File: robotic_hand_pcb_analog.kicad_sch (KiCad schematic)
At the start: 0 parts

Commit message: Add WIP schematic changes
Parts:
- added C25, C26, C28, C29, C30, C31, C32: 100n, Capacitor_SMD:C_0603_1608Metric, symbol Device:C
- added C27: 1u, Capacitor_SMD:C_0603_1608Metric, symbol Device:C
- added C33, C34, C35, C36, C37: 1n, Capacitor_SMD:C_0603_1608Metric, symbol Device:C
- added J10: A5, symbol Connector:Conn_01x03_Pin
- added J11: A6, symbol Connector:Conn_01x03_Pin
- added J12: A7, symbol Connector:Conn_01x03_Pin
- added J13: ISENSE1, Connector_PinHeader_2.54mm:PinHeader_1x02_P2.54mm_Vertical, symbol Connector:Conn_01x02_Pin
- added J14: ISENSE2, Connector_PinHeader_2.54mm:PinHeader_1x02_P2.54mm_Vertical, symbol Connector:Conn_01x02_Pin
- added J15: ISENSE3, Connector_PinHeader_2.54mm:PinHeader_1x02_P2.54mm_Vertical, symbol Connector:Conn_01x02_Pin
- added J16: ISENSE4, Connector_PinHeader_2.54mm:PinHeader_1x02_P2.54mm_Vertical, symbol Connector:Conn_01x02_Pin
- added J17: ISENSE5, Connector_PinHeader_2.54mm:PinHeader_1x02_P2.54mm_Vertical, symbol Connector:Conn_01x02_Pin
- added J6: A1, symbol Connector:Conn_01x03_Pin
- added J7: A2, symbol Connector:Conn_01x03_Pin
- added J8: A3, symbol Connector:Conn_01x03_Pin
- added J9: A4, symbol Connector:Conn_01x03_Pin
- added TP1, TP2, TP3, TP4, TP5: TestPoint, TestPoint:TestPoint_Pad_D2.0mm, symbol Connector:TestPoint
- added U10, U11, U12, U13, U9: ACS712xLCTR-05B, Package_SO:SOIC-8_3.9x4.9mm_P1.27mm, symbol Sensor_Current:ACS712xLCTR-05B
- added U8: ADS114S08, adc:ads114s08_tqfp-32, symbol adc:ads114s08
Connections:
- new net: C34.1, U10.6 (FILTER)
- new net: C36.1, U12.6 (FILTER)
- new net: C37.1, U13.6 (FILTER)
- new net: C35.1, U11.6 (FILTER)
- new net: C33.1, U9.6 (FILTER)
- new net: C27.1, U8.23 (REFOUT)
- new net +3V3: C26.2, U8.15 (IOVDD), U8.16 (DVDD)
- new net +5V: C25.2, C28.2, C29.2, C30.2, C31.2, C32.2, J10.2 (Pin_2), J11.2 (Pin_2), J12.2 (Pin_2), J13.1 (Pin_1), J13.2 (Pin_2), J14.1 (Pin_1), J14.2 (Pin_2), J15.1 (Pin_1), J15.2 (Pin_2), J16.1 (Pin_1), J16.2 (Pin_2), J17.1 (Pin_1), J17.2 (Pin_2), J6.2 (Pin_2), J7.2 (Pin_2), J8.2 (Pin_2), J9.2 (Pin_2), U10.1 (IP+), U10.2 (IP+), U10.3 (IP-), U10.4 (IP-), U10.8 (VCC), U11.1 (IP+), U11.2 (IP+), U11.3 (IP-), U11.4 (IP-), U11.8 (VCC), U12.1 (IP+), U12.2 (IP+), U12.3 (IP-), U12.4 (IP-), U12.8 (VCC), U13.1 (IP+), U13.2 (IP+), U13.3 (IP-), U13.4 (IP-), U13.8 (VCC), U8.26 (AVDD), U9.1 (IP+), U9.2 (IP+), U9.3 (IP-), U9.4 (IP-), U9.8 (VCC)
- new net ADC1: TP1.1, U8.7 (AIN0), U9.7 (VIOUT)
- new net ADC10: J10.1 (Pin_1), U8.21 (GPIO1/AIN9)
- new net ADC11: J11.1 (Pin_1), U8.20 (GPIO2/AIN10)
- new net ADC12: J12.1 (Pin_1), U8.19 (GPIO3/AIN11)
- new net ADC2: TP2.1, U10.7 (VIOUT), U8.6 (AIN1)
- new net ADC3: TP3.1, U11.7 (VIOUT), U8.5 (AIN2)
- new net ADC4: TP4.1, U12.7 (VIOUT), U8.4 (AIN3)
- new net ADC5: TP5.1, U13.7 (VIOUT), U8.3 (AIN4)
- new net ADC6: J6.1 (Pin_1), U8.2 (AIN5)
- new net ADC7: J7.1 (Pin_1), U8.32 (REFP1_AIN6)
- new net ADC8: J8.1 (Pin_1), U8.31 (REFN1_AIN7)
- new net ADC9: J9.1 (Pin_1), U8.22 (GPIO0/AIN8)
- new net ADC_CS: U8.9 (CS_N)
- new net ADC_DRDY: U8.13 (DRDY_N)
- new net ADC_MISO: U8.12 (DOUT/DRDY_N)
- new net ADC_MOSI: U8.10 (DIN)
- new net ADC_RST: U8.18 (RESET_N)
- new net ADC_SCK: U8.11 (SCLK)
- new net ADC_SYNC: U8.8 (START_SYNC)
- new net GND: C25.1, C26.1, C27.2, C28.1, C29.1, C30.1, C31.1, C32.1, C33.2, C34.2, C35.2, C36.2, C37.2, J10.3 (Pin_3), J11.3 (Pin_3), J12.3 (Pin_3), J6.3 (Pin_3), J7.3 (Pin_3), J8.3 (Pin_3), J9.3 (Pin_3), U10.5 (GND), U11.5 (GND), U12.5 (GND), U13.5 (GND), U8.14 (DGND), U8.17 (CLK), U8.24 (REFCOM), U8.27 (AVSS), U8.28 (AVSS), U9.5 (GND)
- no-connect marks 0 -> 3
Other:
- note added: "Current Sensors"
- note added: "External ADC IC"
- note added: "External Analog Sensor Breakouts"

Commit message: Assign footprints
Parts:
- J10, J11, J12, J6, J7, J8, J9: footprint (none) -> Connector_PinHeader_2.54mm:PinHeader_1x03_P2.54mm_Vertical
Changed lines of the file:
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@@
 			)
 		)
-		(property "Footprint" ""
+		(property "Footprint" "Connector_PinHeader_2.54mm:PinHeader_1x03_P2.54mm_Vertical"
 			(at 257.81 38.1 0)
 			(effects
@@
 			)
 		)
-		(property "Footprint" ""
+		(property "Footprint" "Connector_PinHeader_2.54mm:PinHeader_1x03_P2.54mm_Vertical"
 			(at 105.41 38.1 0)
 			(effects
@@
 			)
 		)
-		(property "Footprint" ""
+		(property "Footprint" "Connector_PinHeader_2.54mm:PinHeader_1x03_P2.54mm_Vertical"
 			(at 156.21 38.1 0)
 			(effects
@@
 			)
 		)
-		(property "Footprint" ""
+		(property "Footprint" "Connector_PinHeader_2.54mm:PinHeader_1x03_P2.54mm_Vertical"
 			(at 207.01 38.1 0)
 			(effects
@@
 			)
 		)
-		(property "Footprint" ""
+		(property "Footprint" "Connector_PinHeader_2.54mm:PinHeader_1x03_P2.54mm_Vertical"
 			(at 181.61 38.1 0)
 			(effects
@@
 			)
 		)
-		(property "Footprint" ""
+		(property "Footprint" "Connector_PinHeader_2.54mm:PinHeader_1x03_P2.54mm_Vertical"
 			(at 232.41 38.1 0)
 			(effects
@@
 			)
 		)
-		(property "Footprint" ""
+		(property "Footprint" "Connector_PinHeader_2.54mm:PinHeader_1x03_P2.54mm_Vertical"
 			(at 130.81 38.1 0)
 			(effects

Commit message: Cleanup and remove unneeded connectors
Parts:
- removed J13: ISENSE1, Connector_PinHeader_2.54mm:PinHeader_1x02_P2.54mm_Vertical, symbol Connector:Conn_01x02_Pin
- removed J14: ISENSE2, Connector_PinHeader_2.54mm:PinHeader_1x02_P2.54mm_Vertical, symbol Connector:Conn_01x02_Pin
- removed J15: ISENSE3, Connector_PinHeader_2.54mm:PinHeader_1x02_P2.54mm_Vertical, symbol Connector:Conn_01x02_Pin
- removed J16: ISENSE4, Connector_PinHeader_2.54mm:PinHeader_1x02_P2.54mm_Vertical, symbol Connector:Conn_01x02_Pin
- removed J17: ISENSE5, Connector_PinHeader_2.54mm:PinHeader_1x02_P2.54mm_Vertical, symbol Connector:Conn_01x02_Pin

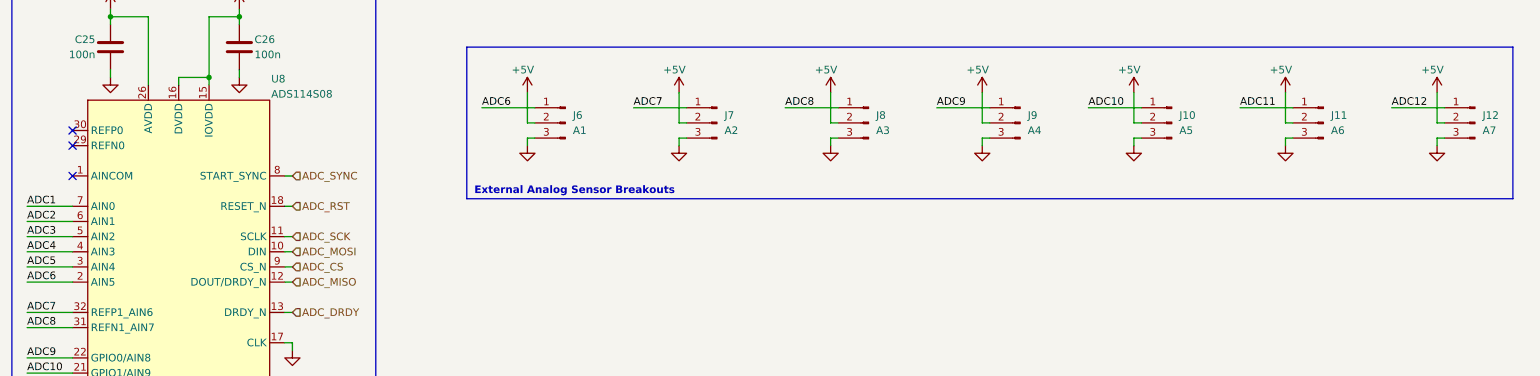
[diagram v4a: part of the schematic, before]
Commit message: Add WIP PCB layout and routing
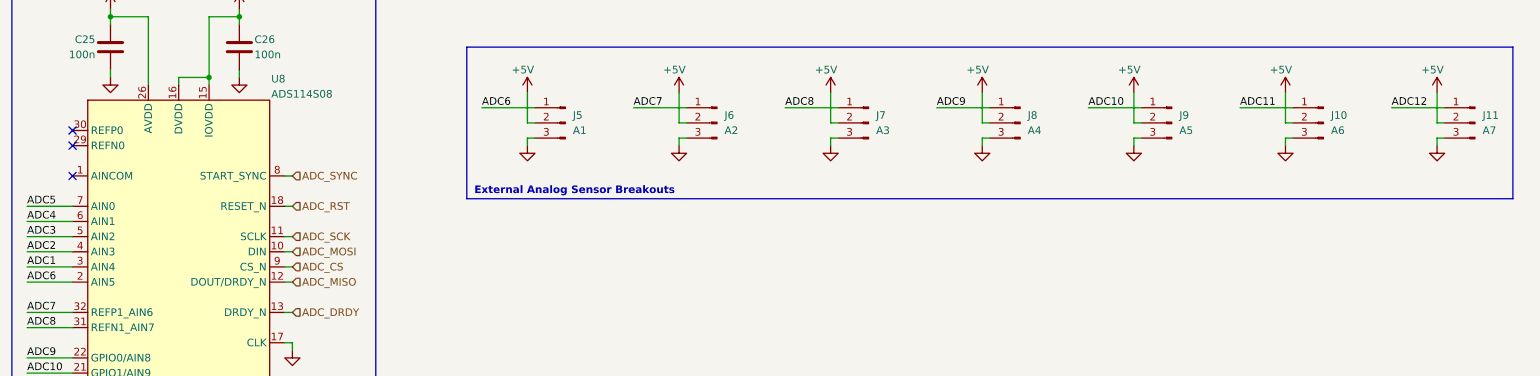
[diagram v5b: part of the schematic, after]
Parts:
- renumbered J11 to J10, J12 to J11, J6 to J5, J7 to J6, J8 to J7, J9 to J8, J10 to J9
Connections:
- net ADC1: now also U8.3 (AIN4); no longer U8.7 (AIN0)
- net ADC2: now also U8.4 (AIN3); no longer U8.6 (AIN1)
- net ADC4: now also U8.6 (AIN1); no longer U8.4 (AIN3)
- net ADC5: now also U8.7 (AIN0); no longer U8.3 (AIN4)

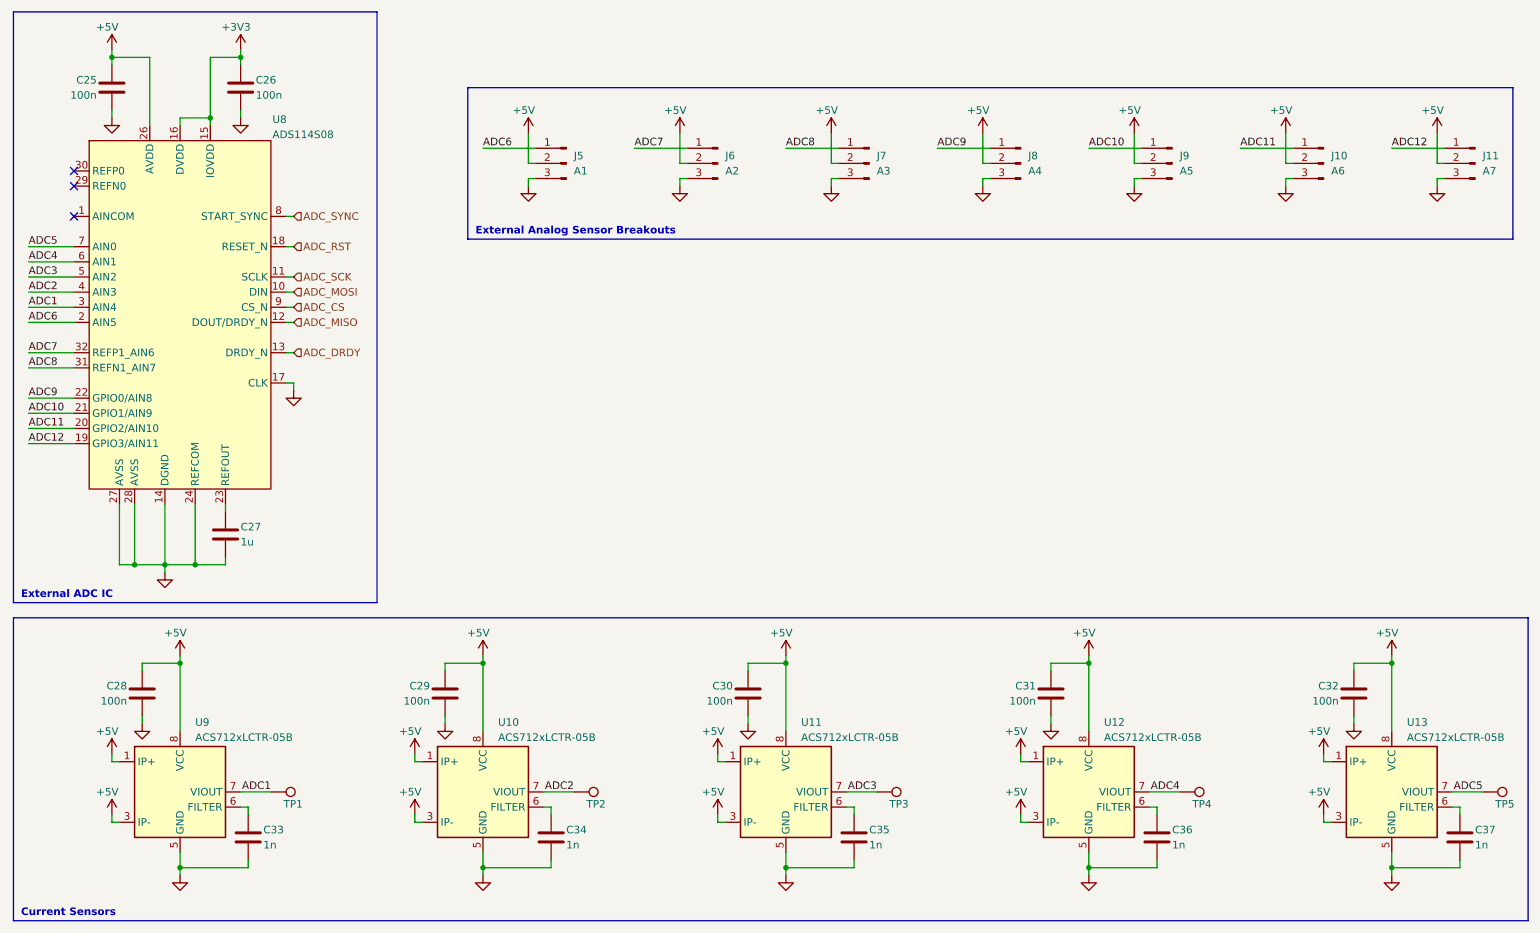
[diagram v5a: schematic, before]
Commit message: Update WIP, clean up stepper drivers
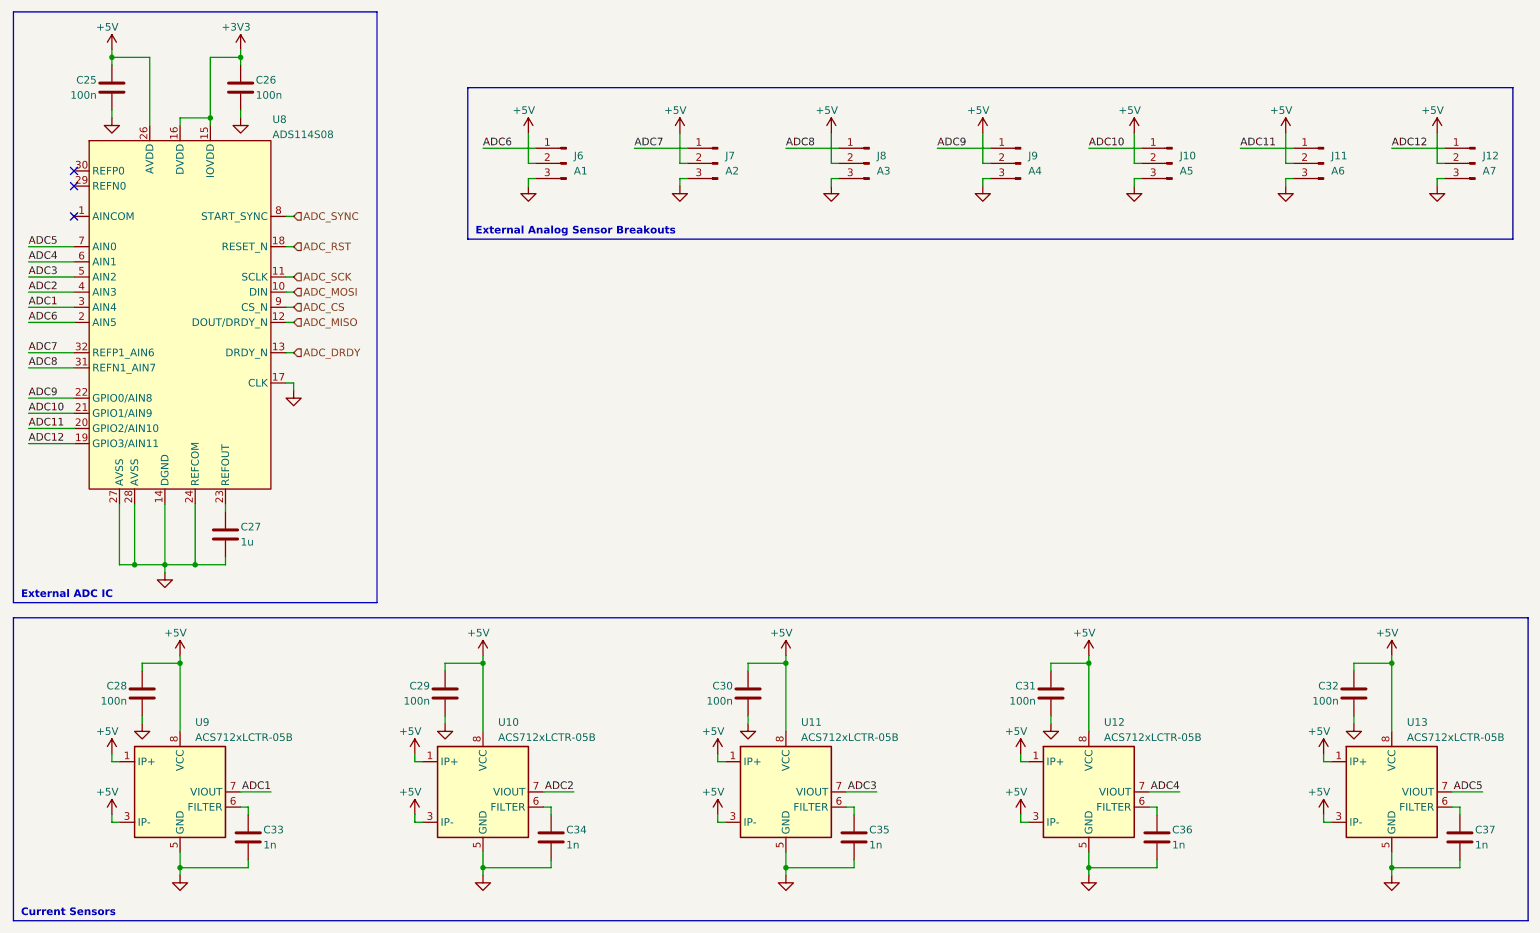
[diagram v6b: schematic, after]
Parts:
- removed TP1, TP2, TP3, TP4, TP5: TestPoint, TestPoint:TestPoint_Pad_D2.0mm, symbol Connector:TestPoint
- renumbered J9 to J10, J10 to J11, J11 to J12, J5 to J6, J6 to J7, J7 to J8, J8 to J9

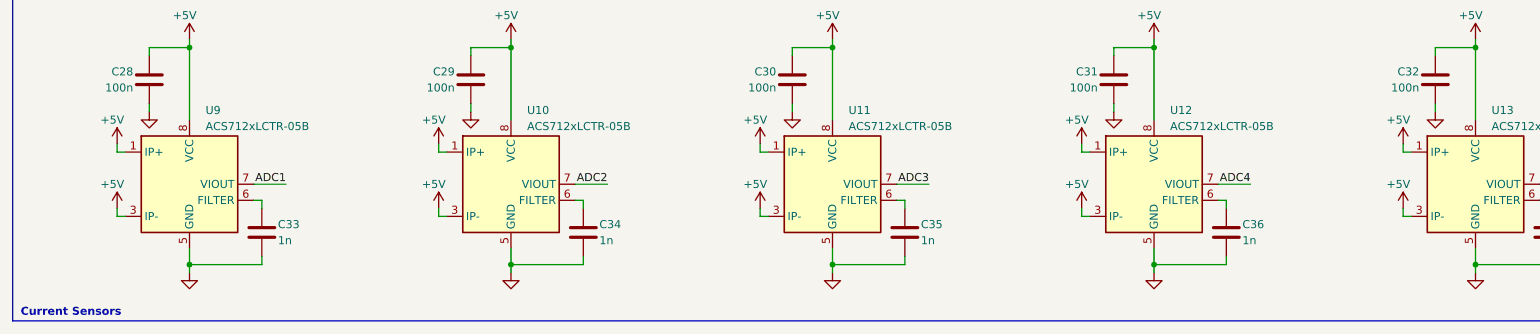
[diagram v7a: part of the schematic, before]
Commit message: Route power, add major cleanup
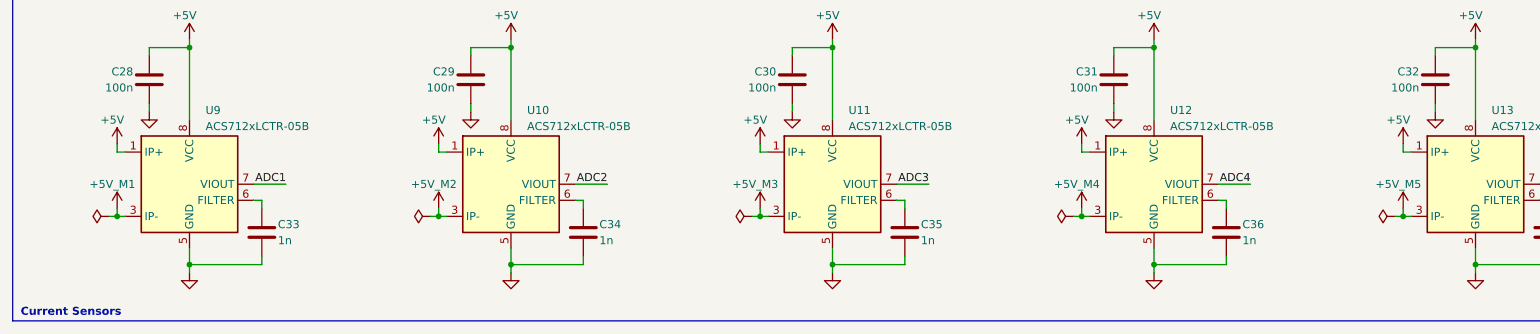
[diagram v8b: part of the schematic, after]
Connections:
- net +5V: no longer U10.3 (IP-), U10.4 (IP-), U11.3 (IP-), U11.4 (IP-), U12.3 (IP-), U12.4 (IP-), U13.3 (IP-), U13.4 (IP-), U9.3 (IP-), U9.4 (IP-)
- new net +5V_M1: U9.3 (IP-), U9.4 (IP-)
- new net +5V_M2: U10.3 (IP-), U10.4 (IP-)
- new net +5V_M3: U11.3 (IP-), U11.4 (IP-)
- new net +5V_M4: U12.3 (IP-), U12.4 (IP-)
- new net +5V_M5: U13.3 (IP-), U13.4 (IP-)
